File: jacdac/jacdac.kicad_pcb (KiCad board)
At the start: 2 copper layers, 60 x 35 mm, 15 parts, among them J1 Conn1, J2 Conn2, J3 Audio_Jack_TRRS, J4 Audio_Jack_TRRS, J5 Audio_Jack_TRRS, J6 Audio_Jack_TRRS

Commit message: version beta testing
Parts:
- added G***: LOGO, Aesthetics:beta_testing, B.Cu at (96.5, 54.8)

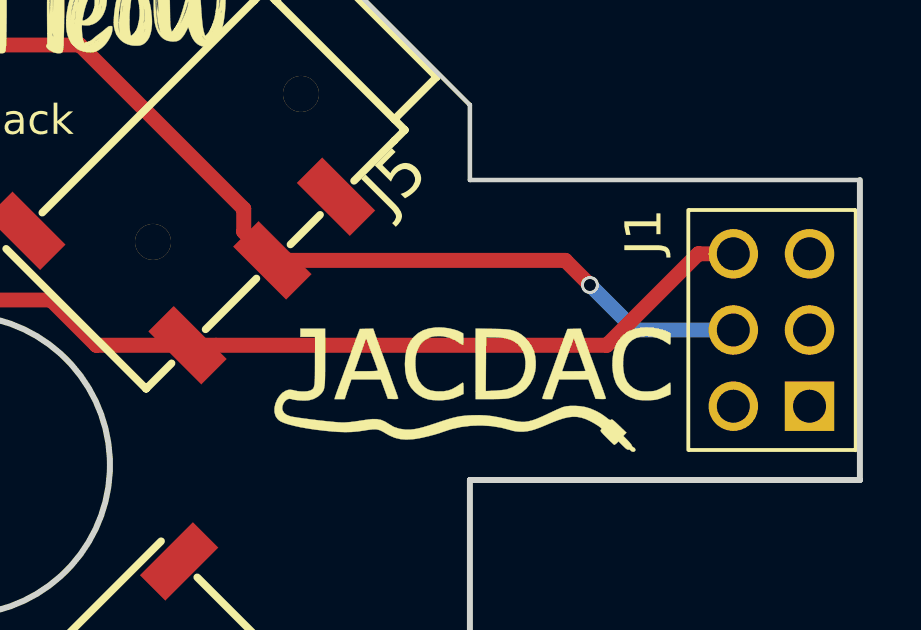
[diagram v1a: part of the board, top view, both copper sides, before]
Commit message: init v0.2 add diodes and resistor
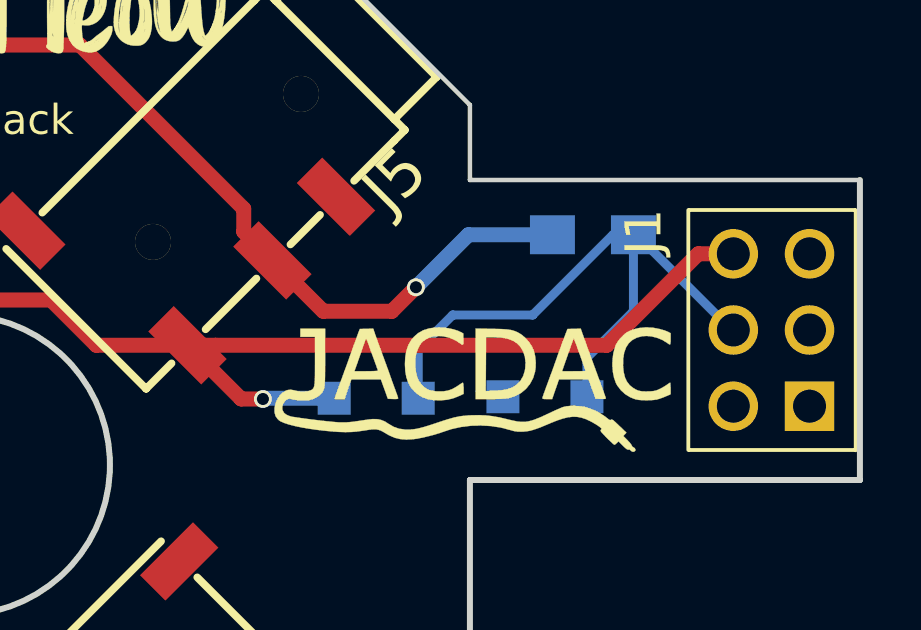
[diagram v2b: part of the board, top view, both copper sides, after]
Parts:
- added D1: MBR120, Diodes_SMD:D_SOD-123F, B.Cu at (122.9, 55.3)
- added D2: MBR120, Diodes_SMD:D_SOD-123F, B.Cu at (128.5, 55.2)
- added R1: 100, Resistors_SMD:R_0805_HandSoldering, B.Cu at (130.1, 49.8)
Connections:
- J1 pad 4: /JACDAC_TX -> Net-(D1-Pad2)
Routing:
- net Net-(D1-Pad2): track 0.00 -> 21.1 mm
- net VCC: track 65.4 -> 71.0 mm, vias 0 -> 1
- net /JACDAC_TX: track 80.5 -> 75.3 mm

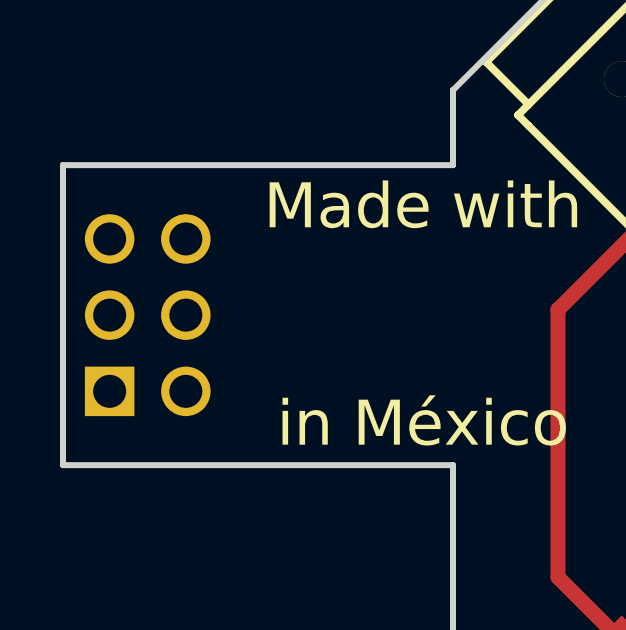
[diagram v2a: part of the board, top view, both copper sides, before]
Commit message: Fix GND inverted
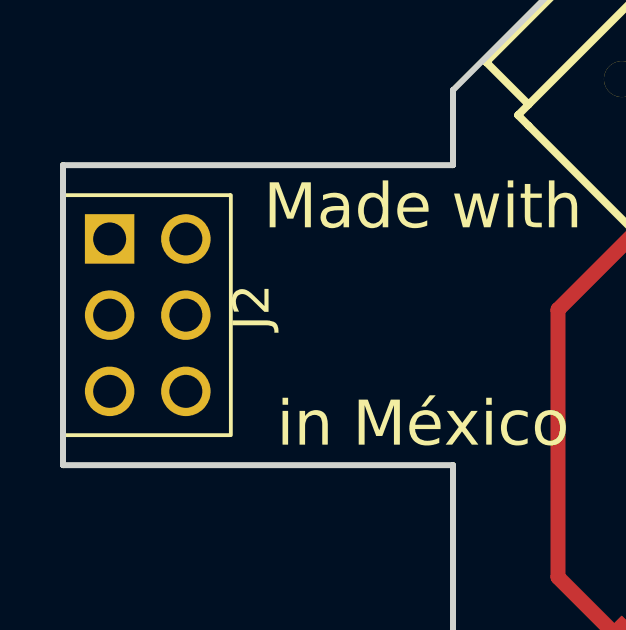
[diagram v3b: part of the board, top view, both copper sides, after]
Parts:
- J2: moved to F.Cu
- turned J2 to 270 degrees
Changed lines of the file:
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@@
   (title_block
     (title JacDac_Cat)
-    (date 2018-12-29)
-    (rev 0.2)
+    (date 2019-03-05)
+    (rev 0.3)
     (company "Electronic Cats")
     (comment 1 "Andres Sabas")
@@
     (pad 3 thru_hole circle (at 1.6 0 225) (size 1.2 1.2) (drill 1.2) (layers *.Cu *.Mask))
   )
-  (module Pines:61300621121 (layer B.Cu)
-    (at 81.825 53 90)
+  (module Pines:61300621121 (layer F.Cu)
+    (at 81.825 53 270)
     (descr "WR-PHD 2.54mm Dual Pin Header, 6 Pins")
-    (fp_text reference J2 (at 0.5 4.175 90) (layer B.SilkS)
-      (effects (font (size 1.2065 1.2065) (thickness 0.1016)) (justify left bottom mirror))
-    )
-    (fp_text value Conn2 (at 6 3.175) (layer F.Fab)
+    (fp_text reference J2 (at 0.5 -4.175 270) (layer F.SilkS)
       (effects (font (size 1.2065 1.2065) (thickness 0.1016)) (justify left bottom))
     )
-    (fp_line (start -4.01 -2.81) (end 3.99 -2.81) (layer B.SilkS) (width 0.127))
-    (fp_line (start 4 2.77) (end -4 2.77) (layer B.SilkS) (width 0.127))
-    (fp_line (start 4 -2.77) (end 4 2.73) (layer B.SilkS) (width 0.127))
-    (fp_line (start -4 -2.77) (end -4 2.73) (layer B.SilkS) (width 0.127))
-    (pad 3 thru_hole circle (at 0 -1.27) (size 1.65 1.65) (drill 1.1) (layers *.Cu *.Mask)
+    (fp_text value Conn2 (at 6 -3.175) (layer B.Fab)
+      (effects (font (size 1.2065 1.2065) (thickness 0.1016)) (justify left bottom mirror))
+    )
+    (fp_line (start -4.01 2.81) (end 3.99 2.81) (layer F.SilkS) (width 0.127))
+    (fp_line (start 4 -2.77) (end -4 -2.77) (layer F.SilkS) (width 0.127))
+    (fp_line (start 4 2.77) (end 4 -2.73) (layer F.SilkS) (width 0.127))
+    (fp_line (start -4 2.77) (end -4 -2.73) (layer F.SilkS) (width 0.127))
+    (pad 3 thru_hole circle (at 0 1.27) (size 1.65 1.65) (drill 1.1) (layers *.Cu *.Mask)
       (net 11 /X3))
-    (pad 4 thru_hole circle (at 0 1.27 180) (size 1.65 1.65) (drill 1.1) (layers *.Cu *.Mask)
+    (pad 4 thru_hole circle (at 0 -1.27 180) (size 1.65 1.65) (drill 1.1) (layers *.Cu *.Mask)
       (net 10 /X2))
-    (pad 6 thru_hole circle (at 2.54 1.27 180) (size 1.65 1.65) (drill 1.1) (layers *.Cu *.Mask)
+    (pad 6 thru_hole circle (at 2.54 -1.27 180) (size 1.65 1.65) (drill 1.1) (layers *.Cu *.Mask)
       (net 8 /I2S_SCK))
-    (pad 1 thru_hole rect (at -2.54 -1.27) (size 1.65 1.65) (drill 1.1) (layers *.Cu *.Mask)
+    (pad 1 thru_hole rect (at -2.54 1.27) (size 1.65 1.65) (drill 1.1) (layers *.Cu *.Mask)
       (net 1 GND))
-    (pad 5 thru_hole circle (at 2.54 -1.27) (size 1.65 1.65) (drill 1.1) (layers *.Cu *.Mask)
+    (pad 5 thru_hole circle (at 2.54 1.27) (size 1.65 1.65) (drill 1.1) (layers *.Cu *.Mask)
       (net 9 /I2S_D1))
-    (pad 2 thru_hole circle (at -2.54 1.27 180) (size 1.65 1.65) (drill 1.1) (layers *.Cu *.Mask)
+    (pad 2 thru_hole circle (at -2.54 -1.27 180) (size 1.65 1.65) (drill 1.1) (layers *.Cu *.Mask)
       (net 12 /CS))
   )
@@
     (connect_pads (clearance 0.508))
     (min_thickness 0.254)
-    (fill (arc_segments 16) (thermal_gap 0.508) (thermal_bridge_width 0.508))
+    (fill yes (arc_segments 16) (thermal_gap 0.508) (thermal_bridge_width 0.508))
     (polygon
       (pts
@@
     (connect_pads (clearance 0.508))
     (min_thickness 0.254)
-    (fill (arc_segments 16) (thermal_gap 0.508) (thermal_bridge_width 0.508))
+    (fill yes (arc_segments 16) (thermal_gap 0.508) (thermal_bridge_width 0.508))
     (polygon
       (pts

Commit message: bump :D
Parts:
- added svg2mod: G***, Aesthetics:heart_trans, B.Cu at (91.1, 53.0)
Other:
- board text added: "v0.3"
- board text removed: "v0.1-beta"
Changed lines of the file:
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@@
     (tracks 56)
     (zones 0)
-    (modules 19)
+    (modules 20)
     (nets 18)
   )
@@
     (46 B.CrtYd user)
     (47 F.CrtYd user)
-    (48 B.Fab user)
-    (49 F.Fab user)
+    (48 B.Fab user hide)
+    (49 F.Fab user hide)
   )
   (setup
@@
       (drillshape 0)
       (scaleselection 1)
-      (outputdirectory "gerbers_betaa/"))
+      (outputdirectory "gerbersv03/"))
   )
   (net 0 "")
@@
     )
   )
+  (module Aesthetics:heart_trans (layer B.Cu)
+    (at 91.059 52.959 180)
+    (descr "Imported from heart.svg")
+    (tags svg2mod)
+    (attr smd)
+    (fp_text reference svg2mod (at 0 5.590896 180) (layer B.SilkS) hide
+      (effects (font (size 1.524 1.524) (thickness 0.3048)) (justify mirror))
+    )
+    (fp_text value G*** (at 0 -5.590896 180) (layer B.SilkS) hide
+      (effects (font (size 1.524 1.524) (thickness 0.3048)) (justify mirror))
+    )
+    (fp_poly (pts (xy -1.48108 2.324304) (xy -1.60345 2.318461) (xy -1.725158 2.300932) (xy -1.844992 2.271718)
+      (xy -1.96185 2.230818) (xy -2.07507 2.178452) (xy -2.183769 2.114291) (xy -2.287067 2.038444)
+      (xy -2.384301 1.95069) (xy -2.472275 1.853456) (xy -2.548123 1.750379) (xy -2.612394 1.641899)
+      (xy -2.66487 1.52879) (xy -2.70577 1.412153) (xy -2.735095 1.292649) (xy -2.752513 1.171382)
+      (xy -2.758356 1.049012) (xy -2.752513 0.926643) (xy -2.735095 0.805265) (xy -2.70588 0.685761)
+      (xy -2.66509 0.569124) (xy -2.612615 0.456125) (xy -2.548343 0.347646) (xy -2.472386 0.244348)
+      (xy -2.380884 0.143255) (xy 0.000035 -2.234356) (xy 2.380955 0.143255) (xy 2.472567 0.244459)
+      (xy 2.548414 0.347536) (xy 2.612465 0.456015) (xy 2.665051 0.569124) (xy 2.705841 0.685872)
+      (xy 2.735165 0.805375) (xy 2.752584 0.926643) (xy 2.758427 1.048902) (xy 2.752584 1.171272)
+      (xy 2.735055 1.292649) (xy 2.705731 1.412153) (xy 2.664941 1.5289) (xy 2.612465 1.641789)
+      (xy 2.548193 1.750379) (xy 2.472236 1.853456) (xy 2.384372 1.95058) (xy 2.287027 2.038444)
+      (xy 2.18373 2.114291) (xy 2.07503 2.178452) (xy 1.96181 2.230818) (xy 1.844953 2.271718)
+      (xy 1.725229 2.300932) (xy 1.603521 2.318461) (xy 1.481041 2.324304) (xy 1.35845 2.318461)
+      (xy 1.236852 2.300932) (xy 1.117128 2.271828) (xy 1.00016 2.231038) (xy 0.88683 2.178563)
+      (xy 0.778241 2.114511) (xy 0.674833 2.038664) (xy 0.57363 1.947383) (xy 0.15625 1.5289)
+      (xy 0.122081 1.500918) (xy 0.084184 1.480902) (xy 0.002157 1.464779) (xy -0.07994 1.48055)
+      (xy -0.117922 1.500404) (xy -0.15221 1.528239) (xy -0.573339 1.947052) (xy -0.674873 2.038664)
+      (xy -0.778281 2.114511) (xy -0.88698 2.178673) (xy -1.00009 2.231038) (xy -1.116947 2.271828)
+      (xy -1.236892 2.300932) (xy -1.35849 2.318461) (xy -1.48108 2.324304)) (layer B.Mask) (width 0))
+    (fp_poly (pts (xy 0 -2.542896) (xy -2.53909 -0.007352) (xy -2.641746 0.106128) (xy -2.730712 0.227037)
+      (xy -2.805987 0.354313) (xy -2.867572 0.486894) (xy -2.915467 0.623719) (xy -2.949671 0.763727)
+      (xy -2.970186 0.905855) (xy -2.97701 1.049043) (xy -2.970145 1.192229) (xy -2.94959 1.334351)
+      (xy -2.915346 1.474348) (xy -2.867413 1.611159) (xy -2.80579 1.743721) (xy -2.730479 1.870975)
+      (xy -2.641479 1.991857) (xy -2.53879 2.105306) (xy -2.425181 2.207848) (xy -2.30413 2.296721)
+      (xy -2.176698 2.371924) (xy -2.04395 2.433458) (xy -1.906947 2.481322) (xy -1.766754 2.515517)
+      (xy -1.624433 2.536042) (xy -1.481047 2.542896) (xy -1.337658 2.536081) (xy -1.195331 2.515595)
+      (xy -1.055128 2.481438) (xy -0.918112 2.43361) (xy -0.785346 2.372112) (xy -0.657893 2.296942)
+      (xy -0.536816 2.2081) (xy -0.423178 2.105588) (xy 0.001659 1.683002) (xy 0.423178 2.105588)
+      (xy 0.536816 2.2081) (xy 0.657893 2.296942) (xy 0.785346 2.372111) (xy 0.918112 2.43361)
+      (xy 1.055128 2.481437) (xy 1.195331 2.515594) (xy 1.337658 2.536079) (xy 1.481047 2.542894)
+      (xy 1.624433 2.536038) (xy 1.766754 2.515512) (xy 1.906948 2.481316) (xy 2.04395 2.43345)
+      (xy 2.176699 2.371914) (xy 2.304131 2.296708) (xy 2.425183 2.207833) (xy 2.538792 2.105288)
+      (xy 2.64148 1.991838) (xy 2.73048 1.870956) (xy 2.805791 1.743703) (xy 2.867413 1.61114)
+      (xy 2.915347 1.47433) (xy 2.94959 1.334333) (xy 2.970145 1.192211) (xy 2.97701 1.049025)
+      (xy 2.970186 0.905838) (xy 2.949672 0.76371) (xy 2.915467 0.623704) (xy 2.867573 0.486879)
+      (xy 2.805988 0.354299) (xy 2.730713 0.227025) (xy 2.641747 0.106118) (xy 2.539091 -0.007361)
+      (xy 0 -2.542896)) (layer B.Mask) (width 0.094249))
+  )
   (dimension 60.07602 (width 0.3) (layer Margin)
     (gr_text "60,076 mm" (at 108.802296 22.52697 0.3338043436) (layer Margin)
@@
     (effects (font (size 1 1) (thickness 0.25)) (justify mirror))
   )
-  (gr_text v0.1-beta (at 112.5 51.5) (layer B.SilkS)
+  (gr_text v0.3 (at 112.5 51.5) (layer B.SilkS)
     (effects (font (size 1 1) (thickness 0.25)) (justify mirror))
   )
